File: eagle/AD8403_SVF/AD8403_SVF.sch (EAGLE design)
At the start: 30 parts, among them IC1 AD8403-DIP24, IC2 NJM2732, IC3 NJM2732

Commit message: Update: eagle files
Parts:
- added JP8: GND, pinhead:PINHD-1X2
- R7, R8: device rcl:R-EU_0207/7 -> rcl:R-EU_0204/2V
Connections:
- removed net N$15: LED1.C, R7.2
- new net N$13: LED1.A, R7.1
- net +5V: now also R7.2; no longer LED1.A
- net GND: now also JP4.2, JP5.2, JP6.2, JP8.1, JP8.2
- net VCC/2: now also LED1.C; no longer JP4.2, JP5.2, JP6.2, R7.1
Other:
- moved on the sheet: LED1, R7
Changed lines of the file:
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@@
 <part name="C8" library="rcl" deviceset="CPOL-EU" device="E2.5-7" value="100uF"/>
 <part name="C9" library="rcl" deviceset="CPOL-EU" device="E2.5-7" value="100uF"/>
-<part name="P+9" library="supply1" deviceset="VCC/2" device="" value="VGND"/>
 <part name="P+10" library="supply1" deviceset="VCC/2" device="" value="VGND"/>
 <part name="C10" library="rcl" deviceset="C-EU" device="050-055X075" value="2.2uF"/>
@@
 <part name="LED1" library="led" deviceset="LED" device="3MM" value="red"/>
 <part name="LED2" library="led" deviceset="LED" device="3MM" value="red"/>
-<part name="R7" library="rcl" deviceset="R-EU_" device="0207/7" value="220"/>
-<part name="R8" library="rcl" deviceset="R-EU_" device="0207/7" value="220"/>
+<part name="R7" library="rcl" deviceset="R-EU_" device="0204/2V" value="220"/>
+<part name="R8" library="rcl" deviceset="R-EU_" device="0204/2V" value="220"/>
 <part name="P+13" library="supply1" deviceset="VCC/2" device="" value="VGND"/>
 <part name="GND3" library="supply1" deviceset="GND" device=""/>
@@
 <part name="P+3" library="supply1" deviceset="VCC/2" device="" value="VGND"/>
 <part name="GND6" library="supply1" deviceset="GND" device=""/>
+<part name="GND7" library="supply1" deviceset="GND" device=""/>
+<part name="JP8" library="pinhead" deviceset="PINHD-1X2" device="" value="GND"/>
+<part name="GND9" library="supply1" deviceset="GND" device=""/>
 </parts>
 <sheets>
@@
 <instance part="C8" gate="G$1" x="78.74" y="152.4"/>
 <instance part="C9" gate="G$1" x="78.74" y="139.7"/>
-<instance part="P+9" gate="G$1" x="223.52" y="91.44" rot="R180"/>
 <instance part="P+10" gate="G$1" x="210.82" y="55.88" rot="R180"/>
 <instance part="C10" gate="G$1" x="66.04" y="106.68" rot="R90"/>
@@
 <instance part="FRAME1" gate="G$1" x="0" y="0"/>
 <instance part="R6" gate="G$1" x="119.38" y="86.36"/>
-<instance part="LED1" gate="G$1" x="25.4" y="58.42"/>
+<instance part="LED1" gate="G$1" x="25.4" y="45.72"/>
 <instance part="LED2" gate="G$1" x="38.1" y="58.42"/>
-<instance part="R7" gate="G$1" x="25.4" y="45.72" rot="R90"/>
+<instance part="R7" gate="G$1" x="25.4" y="55.88" rot="R90"/>
 <instance part="R8" gate="G$1" x="38.1" y="45.72" rot="R90"/>
 <instance part="P+13" gate="G$1" x="25.4" y="35.56" rot="R180"/>
@@
 <instance part="P+3" gate="G$1" x="76.2" y="78.74"/>
 <instance part="GND6" gate="1" x="45.72" y="88.9"/>
+<instance part="GND7" gate="1" x="223.52" y="91.44"/>
+<instance part="JP8" gate="G$1" x="193.04" y="40.64"/>
+<instance part="GND9" gate="1" x="185.42" y="33.02"/>
 </instances>
 <busses>
@@
 </segment>
 <segment>
-<pinref part="R8" gate="G$1" pin="1"/>
-<pinref part="GND3" gate="1" pin="GND"/>
-<wire x1="38.1" y1="40.64" x2="38.1" y2="38.1" width="0.1524" layer="91"/>
-</segment>
-<segment>
 <pinref part="JP3" gate="G$1" pin="2"/>
 <wire x1="45.72" y1="111.76" x2="38.1" y2="111.76" width="0.1524" layer="91"/>
@@
 <wire x1="55.88" y1="96.52" x2="55.88" y2="101.6" width="0.1524" layer="91"/>
 <pinref part="GND6" gate="1" pin="GND"/>
+</segment>
+<segment>
+<pinref part="JP4" gate="G$1" pin="2"/>
+<wire x1="231.14" y1="101.6" x2="223.52" y2="101.6" width="0.1524" layer="91"/>
+<wire x1="223.52" y1="93.98" x2="223.52" y2="101.6" width="0.1524" layer="91"/>
+<pinref part="JP5" gate="G$1" pin="2"/>
+<wire x1="231.14" y1="124.46" x2="223.52" y2="124.46" width="0.1524" layer="91"/>
+<wire x1="223.52" y1="124.46" x2="223.52" y2="101.6" width="0.1524" layer="91"/>
+<junction x="223.52" y="101.6"/>
+<pinref part="JP6" gate="G$1" pin="2"/>
+<wire x1="231.14" y1="139.7" x2="223.52" y2="139.7" width="0.1524" layer="91"/>
+<wire x1="223.52" y1="139.7" x2="223.52" y2="124.46" width="0.1524" layer="91"/>
+<junction x="223.52" y="124.46"/>
+<pinref part="GND7" gate="1" pin="GND"/>
+</segment>
+<segment>
+<pinref part="JP8" gate="G$1" pin="1"/>
+<wire x1="190.5" y1="43.18" x2="185.42" y2="43.18" width="0.1524" layer="91"/>
+<wire x1="185.42" y1="43.18" x2="185.42" y2="40.64" width="0.1524" layer="91"/>
+<pinref part="JP8" gate="G$1" pin="2"/>
+<wire x1="185.42" y1="40.64" x2="190.5" y2="40.64" width="0.1524" layer="91"/>
+<wire x1="185.42" y1="40.64" x2="185.42" y2="35.56" width="0.1524" layer="91"/>
+<junction x="185.42" y="40.64"/>
+<pinref part="GND9" gate="1" pin="GND"/>
+</segment>
+<segment>
+<pinref part="GND3" gate="1" pin="GND"/>
+<pinref part="R8" gate="G$1" pin="1"/>
+<wire x1="38.1" y1="38.1" x2="38.1" y2="40.64" width="0.1524" layer="91"/>
 </segment>
 </net>
@@
 </segment>
 <segment>
-<pinref part="LED1" gate="G$1" pin="A"/>
+<pinref part="R7" gate="G$1" pin="2"/>
 <pinref part="P+15" gate="1" pin="+5V"/>
 <wire x1="25.4" y1="60.96" x2="25.4" y2="63.5" width="0.1524" layer="91"/>
@@
 </segment>
 <segment>
-<pinref part="JP4" gate="G$1" pin="2"/>
-<wire x1="231.14" y1="101.6" x2="223.52" y2="101.6" width="0.1524" layer="91"/>
-<wire x1="223.52" y1="93.98" x2="223.52" y2="101.6" width="0.1524" layer="91"/>
-<pinref part="JP5" gate="G$1" pin="2"/>
-<wire x1="231.14" y1="124.46" x2="223.52" y2="124.46" width="0.1524" layer="91"/>
-<wire x1="223.52" y1="124.46" x2="223.52" y2="101.6" width="0.1524" layer="91"/>
-<junction x="223.52" y="101.6"/>
-<pinref part="JP6" gate="G$1" pin="2"/>
-<wire x1="231.14" y1="139.7" x2="223.52" y2="139.7" width="0.1524" layer="91"/>
-<wire x1="223.52" y1="139.7" x2="223.52" y2="124.46" width="0.1524" layer="91"/>
-<junction x="223.52" y="124.46"/>
-<pinref part="P+9" gate="G$1" pin="VCC/2"/>
-</segment>
-<segment>
 <wire x1="210.82" y1="63.5" x2="210.82" y2="58.42" width="0.1524" layer="91"/>
 <pinref part="P+10" gate="G$1" pin="VCC/2"/>
@@
 <pinref part="R4" gate="G$1" pin="1"/>
 <wire x1="76.2" y1="91.44" x2="76.2" y2="93.98" width="0.1524" layer="91"/>
-</segment>
-<segment>
-<pinref part="LED2" gate="G$1" pin="A"/>
-<pinref part="P+14" gate="G$1" pin="VCC/2"/>
-<wire x1="38.1" y1="60.96" x2="38.1" y2="63.5" width="0.1524" layer="91"/>
-</segment>
-<segment>
-<pinref part="R7" gate="G$1" pin="1"/>
-<pinref part="P+13" gate="G$1" pin="VCC/2"/>
-<wire x1="25.4" y1="40.64" x2="25.4" y2="38.1" width="0.1524" layer="91"/>
 </segment>
 <segment>
@@
 <label x="68.58" y="43.18" size="1.778" layer="95"/>
 </segment>
+<segment>
+<pinref part="LED1" gate="G$1" pin="C"/>
+<pinref part="P+13" gate="G$1" pin="VCC/2"/>
+<wire x1="25.4" y1="40.64" x2="25.4" y2="38.1" width="0.1524" layer="91"/>
+</segment>
+<segment>
+<pinref part="LED2" gate="G$1" pin="A"/>
+<pinref part="P+14" gate="G$1" pin="VCC/2"/>
+<wire x1="38.1" y1="60.96" x2="38.1" y2="63.5" width="0.1524" layer="91"/>
+</segment>
 </net>
 <net name="N$1" class="0">
@@
 </segment>
 </net>
+<net name="N$13" class="0">
+<segment>
+<pinref part="R7" gate="G$1" pin="1"/>
+<pinref part="LED1" gate="G$1" pin="A"/>
+<wire x1="25.4" y1="50.8" x2="25.4" y2="48.26" width="0.1524" layer="91"/>
+</segment>
+</net>
 <net name="N$14" class="0">
 <segment>
+<pinref part="R8" gate="G$1" pin="2"/>
 <pinref part="LED2" gate="G$1" pin="C"/>
-<pinref part="R8" gate="G$1" pin="2"/>
-<wire x1="38.1" y1="53.34" x2="38.1" y2="50.8" width="0.1524" layer="91"/>
-</segment>
-</net>
-<net name="N$15" class="0">
-<segment>
-<pinref part="LED1" gate="G$1" pin="C"/>
-<pinref part="R7" gate="G$1" pin="2"/>
-<wire x1="25.4" y1="53.34" x2="25.4" y2="50.8" width="0.1524" layer="91"/>
-</segment>
-</net>
+<wire x1="38.1" y1="50.8" x2="38.1" y2="53.34" width="0.1524" layer="91"/>
+</segment>
+</net>

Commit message: Update: eagle files
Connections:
- net +5V: now also IC1.!RS, R7.1; no longer R7.2
- net GND: no longer IC1.!RS, JP4.2, JP5.2, JP6.2
- net N$13: now also R7.2; no longer R7.1
- net VCC/2: now also JP4.2, JP5.2, JP6.2
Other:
- moved on the sheet: R7
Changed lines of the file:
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@@
 <part name="P+3" library="supply1" deviceset="VCC/2" device="" value="VGND"/>
 <part name="GND6" library="supply1" deviceset="GND" device=""/>
-<part name="GND7" library="supply1" deviceset="GND" device=""/>
 <part name="JP8" library="pinhead" deviceset="PINHD-1X2" device="" value="GND"/>
 <part name="GND9" library="supply1" deviceset="GND" device=""/>
+<part name="P+9" library="supply1" deviceset="VCC/2" device="" value="VGND"/>
 </parts>
 <sheets>
@@
 <instance part="LED1" gate="G$1" x="25.4" y="45.72"/>
 <instance part="LED2" gate="G$1" x="38.1" y="58.42"/>
-<instance part="R7" gate="G$1" x="25.4" y="55.88" rot="R90"/>
+<instance part="R7" gate="G$1" x="25.4" y="55.88" rot="R270"/>
 <instance part="R8" gate="G$1" x="38.1" y="45.72" rot="R90"/>
 <instance part="P+13" gate="G$1" x="25.4" y="35.56" rot="R180"/>
@@
 <instance part="P+3" gate="G$1" x="76.2" y="78.74"/>
 <instance part="GND6" gate="1" x="45.72" y="88.9"/>
-<instance part="GND7" gate="1" x="223.52" y="91.44"/>
 <instance part="JP8" gate="G$1" x="193.04" y="40.64"/>
 <instance part="GND9" gate="1" x="185.42" y="33.02"/>
+<instance part="P+9" gate="G$1" x="223.52" y="91.44" rot="R180"/>
 </instances>
 <busses>
@@
 <wire x1="91.44" y1="20.32" x2="137.16" y2="20.32" width="0.1524" layer="91"/>
 <junction x="91.44" y="20.32"/>
-<wire x1="137.16" y1="20.32" x2="137.16" y2="45.72" width="0.1524" layer="91"/>
+<wire x1="137.16" y1="20.32" x2="137.16" y2="50.8" width="0.1524" layer="91"/>
 <pinref part="IC1" gate="G$1" pin="AGND1"/>
-<wire x1="137.16" y1="45.72" x2="137.16" y2="50.8" width="0.1524" layer="91"/>
 <wire x1="137.16" y1="50.8" x2="137.16" y2="60.96" width="0.1524" layer="91"/>
 <wire x1="137.16" y1="60.96" x2="132.08" y2="60.96" width="0.1524" layer="91"/>
@@
 <wire x1="132.08" y1="50.8" x2="137.16" y2="50.8" width="0.1524" layer="91"/>
 <junction x="137.16" y="50.8"/>
-<pinref part="IC1" gate="G$1" pin="!RS"/>
-<wire x1="132.08" y1="45.72" x2="137.16" y2="45.72" width="0.1524" layer="91"/>
-<junction x="137.16" y="45.72"/>
 <wire x1="91.44" y1="20.32" x2="63.5" y2="20.32" width="0.1524" layer="91"/>
 <pinref part="JP1" gate="A" pin="4"/>
@@
 </segment>
 <segment>
-<pinref part="JP4" gate="G$1" pin="2"/>
-<wire x1="231.14" y1="101.6" x2="223.52" y2="101.6" width="0.1524" layer="91"/>
-<wire x1="223.52" y1="93.98" x2="223.52" y2="101.6" width="0.1524" layer="91"/>
-<pinref part="JP5" gate="G$1" pin="2"/>
-<wire x1="231.14" y1="124.46" x2="223.52" y2="124.46" width="0.1524" layer="91"/>
-<wire x1="223.52" y1="124.46" x2="223.52" y2="101.6" width="0.1524" layer="91"/>
-<junction x="223.52" y="101.6"/>
-<pinref part="JP6" gate="G$1" pin="2"/>
-<wire x1="231.14" y1="139.7" x2="223.52" y2="139.7" width="0.1524" layer="91"/>
-<wire x1="223.52" y1="139.7" x2="223.52" y2="124.46" width="0.1524" layer="91"/>
-<junction x="223.52" y="124.46"/>
-<pinref part="GND7" gate="1" pin="GND"/>
-</segment>
-<segment>
 <pinref part="JP8" gate="G$1" pin="1"/>
 <wire x1="190.5" y1="43.18" x2="185.42" y2="43.18" width="0.1524" layer="91"/>
@@
 <segment>
 <pinref part="IC1" gate="G$1" pin="VDD"/>
-<wire x1="132.08" y1="48.26" x2="142.24" y2="48.26" width="0.1524" layer="91"/>
+<wire x1="132.08" y1="48.26" x2="134.62" y2="48.26" width="0.1524" layer="91"/>
+<wire x1="134.62" y1="48.26" x2="142.24" y2="48.26" width="0.1524" layer="91"/>
 <wire x1="142.24" y1="48.26" x2="142.24" y2="76.2" width="0.1524" layer="91"/>
 <pinref part="P+2" gate="1" pin="+5V"/>
@@
 <wire x1="142.24" y1="45.72" x2="142.24" y2="48.26" width="0.1524" layer="91"/>
 <junction x="142.24" y="48.26"/>
+<pinref part="IC1" gate="G$1" pin="!RS"/>
+<wire x1="132.08" y1="45.72" x2="134.62" y2="45.72" width="0.1524" layer="91"/>
+<wire x1="134.62" y1="45.72" x2="134.62" y2="48.26" width="0.1524" layer="91"/>
+<junction x="134.62" y="48.26"/>
 </segment>
 <segment>
@@
 </segment>
 <segment>
-<pinref part="R7" gate="G$1" pin="2"/>
+<pinref part="R7" gate="G$1" pin="1"/>
 <pinref part="P+15" gate="1" pin="+5V"/>
 <wire x1="25.4" y1="60.96" x2="25.4" y2="63.5" width="0.1524" layer="91"/>
@@
 <wire x1="38.1" y1="60.96" x2="38.1" y2="63.5" width="0.1524" layer="91"/>
 </segment>
+<segment>
+<pinref part="JP4" gate="G$1" pin="2"/>
+<wire x1="231.14" y1="101.6" x2="223.52" y2="101.6" width="0.1524" layer="91"/>
+<wire x1="223.52" y1="93.98" x2="223.52" y2="101.6" width="0.1524" layer="91"/>
+<pinref part="JP5" gate="G$1" pin="2"/>
+<wire x1="231.14" y1="124.46" x2="223.52" y2="124.46" width="0.1524" layer="91"/>
+<wire x1="223.52" y1="124.46" x2="223.52" y2="101.6" width="0.1524" layer="91"/>
+<junction x="223.52" y="101.6"/>
+<pinref part="JP6" gate="G$1" pin="2"/>
+<wire x1="231.14" y1="139.7" x2="223.52" y2="139.7" width="0.1524" layer="91"/>
+<wire x1="223.52" y1="139.7" x2="223.52" y2="124.46" width="0.1524" layer="91"/>
+<junction x="223.52" y="124.46"/>
+<pinref part="P+9" gate="G$1" pin="VCC/2"/>
+</segment>
 </net>
 <net name="N$1" class="0">
@@
 </segment>
 </net>
-<net name="N$13" class="0">
-<segment>
-<pinref part="R7" gate="G$1" pin="1"/>
-<pinref part="LED1" gate="G$1" pin="A"/>
-<wire x1="25.4" y1="50.8" x2="25.4" y2="48.26" width="0.1524" layer="91"/>
-</segment>
-</net>
 <net name="N$14" class="0">
 <segment>
@@
 </segment>
 </net>
+<net name="N$13" class="0">
+<segment>
+<pinref part="R7" gate="G$1" pin="2"/>
+<pinref part="LED1" gate="G$1" pin="A"/>
+<wire x1="25.4" y1="50.8" x2="25.4" y2="48.26" width="0.1524" layer="91"/>
+</segment>
+</net>

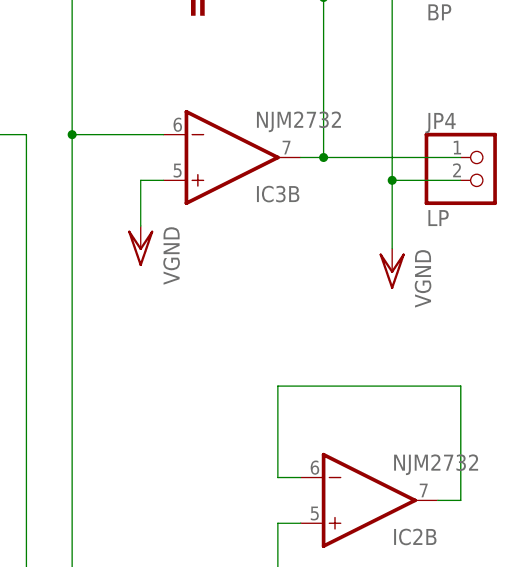
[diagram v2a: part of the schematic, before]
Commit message: change the output GND from VGND to GND
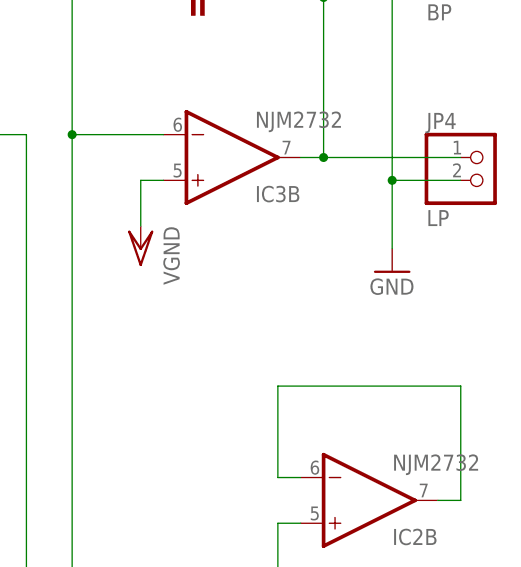
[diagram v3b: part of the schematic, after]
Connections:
- net GND: now also JP4.2, JP5.2, JP6.2
- net VCC/2: no longer JP4.2, JP5.2, JP6.2
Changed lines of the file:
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@@
 <part name="JP8" library="pinhead" deviceset="PINHD-1X2" device="" value="GND"/>
 <part name="GND9" library="supply1" deviceset="GND" device=""/>
-<part name="P+9" library="supply1" deviceset="VCC/2" device="" value="VGND"/>
+<part name="GND7" library="supply1" deviceset="GND" device=""/>
 </parts>
 <sheets>
@@
 <instance part="JP8" gate="G$1" x="193.04" y="40.64"/>
 <instance part="GND9" gate="1" x="185.42" y="33.02"/>
-<instance part="P+9" gate="G$1" x="223.52" y="91.44" rot="R180"/>
+<instance part="GND7" gate="1" x="223.52" y="91.44"/>
 </instances>
 <busses>
@@
 <wire x1="38.1" y1="38.1" x2="38.1" y2="40.64" width="0.1524" layer="91"/>
 </segment>
+<segment>
+<pinref part="JP4" gate="G$1" pin="2"/>
+<wire x1="231.14" y1="101.6" x2="223.52" y2="101.6" width="0.1524" layer="91"/>
+<wire x1="223.52" y1="93.98" x2="223.52" y2="101.6" width="0.1524" layer="91"/>
+<pinref part="JP5" gate="G$1" pin="2"/>
+<wire x1="231.14" y1="124.46" x2="223.52" y2="124.46" width="0.1524" layer="91"/>
+<wire x1="223.52" y1="124.46" x2="223.52" y2="101.6" width="0.1524" layer="91"/>
+<junction x="223.52" y="101.6"/>
+<pinref part="JP6" gate="G$1" pin="2"/>
+<wire x1="231.14" y1="139.7" x2="223.52" y2="139.7" width="0.1524" layer="91"/>
+<wire x1="223.52" y1="139.7" x2="223.52" y2="124.46" width="0.1524" layer="91"/>
+<junction x="223.52" y="124.46"/>
+<pinref part="GND7" gate="1" pin="GND"/>
+</segment>
 </net>
 <net name="+5V" class="0">
@@
 <wire x1="38.1" y1="60.96" x2="38.1" y2="63.5" width="0.1524" layer="91"/>
 </segment>
-<segment>
-<pinref part="JP4" gate="G$1" pin="2"/>
-<wire x1="231.14" y1="101.6" x2="223.52" y2="101.6" width="0.1524" layer="91"/>
-<wire x1="223.52" y1="93.98" x2="223.52" y2="101.6" width="0.1524" layer="91"/>
-<pinref part="JP5" gate="G$1" pin="2"/>
-<wire x1="231.14" y1="124.46" x2="223.52" y2="124.46" width="0.1524" layer="91"/>
-<wire x1="223.52" y1="124.46" x2="223.52" y2="101.6" width="0.1524" layer="91"/>
-<junction x="223.52" y="101.6"/>
-<pinref part="JP6" gate="G$1" pin="2"/>
-<wire x1="231.14" y1="139.7" x2="223.52" y2="139.7" width="0.1524" layer="91"/>
-<wire x1="223.52" y1="139.7" x2="223.52" y2="124.46" width="0.1524" layer="91"/>
-<junction x="223.52" y="124.46"/>
-<pinref part="P+9" gate="G$1" pin="VCC/2"/>
-</segment>
-</net>
+</net>
